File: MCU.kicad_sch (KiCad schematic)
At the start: 14 parts, among them U6 STM32F103RBTx, X1 CSTNE8M00G520000R0

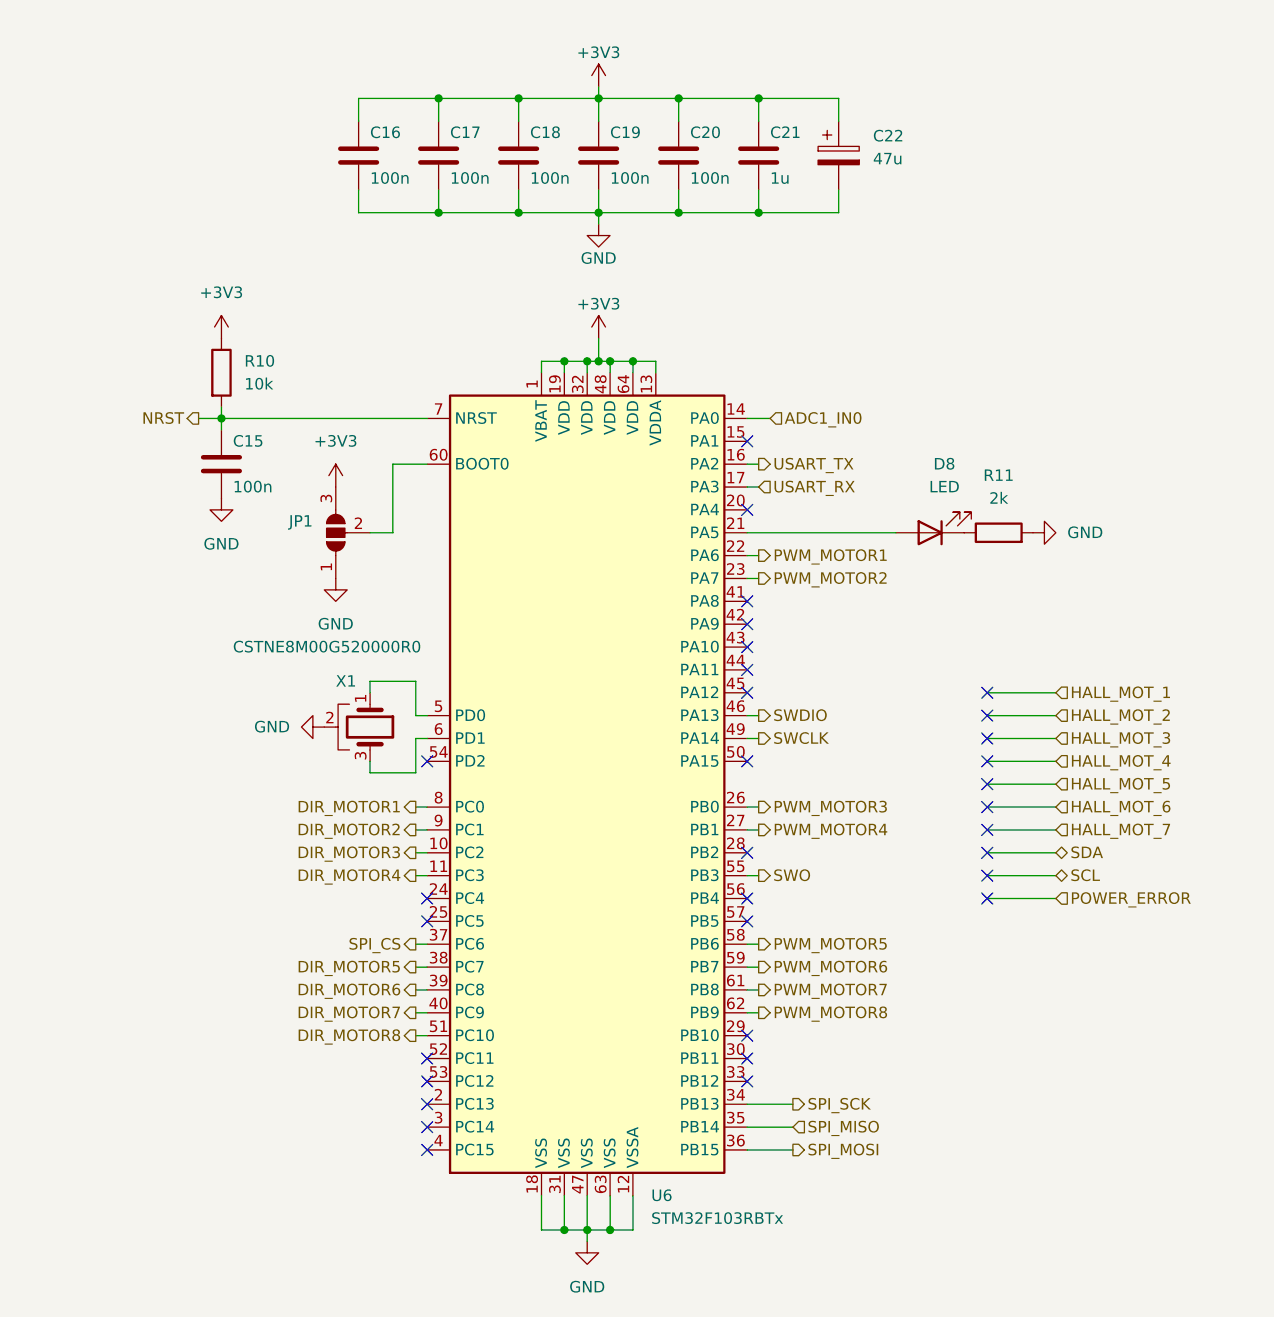
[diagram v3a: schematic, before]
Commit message: power part designed
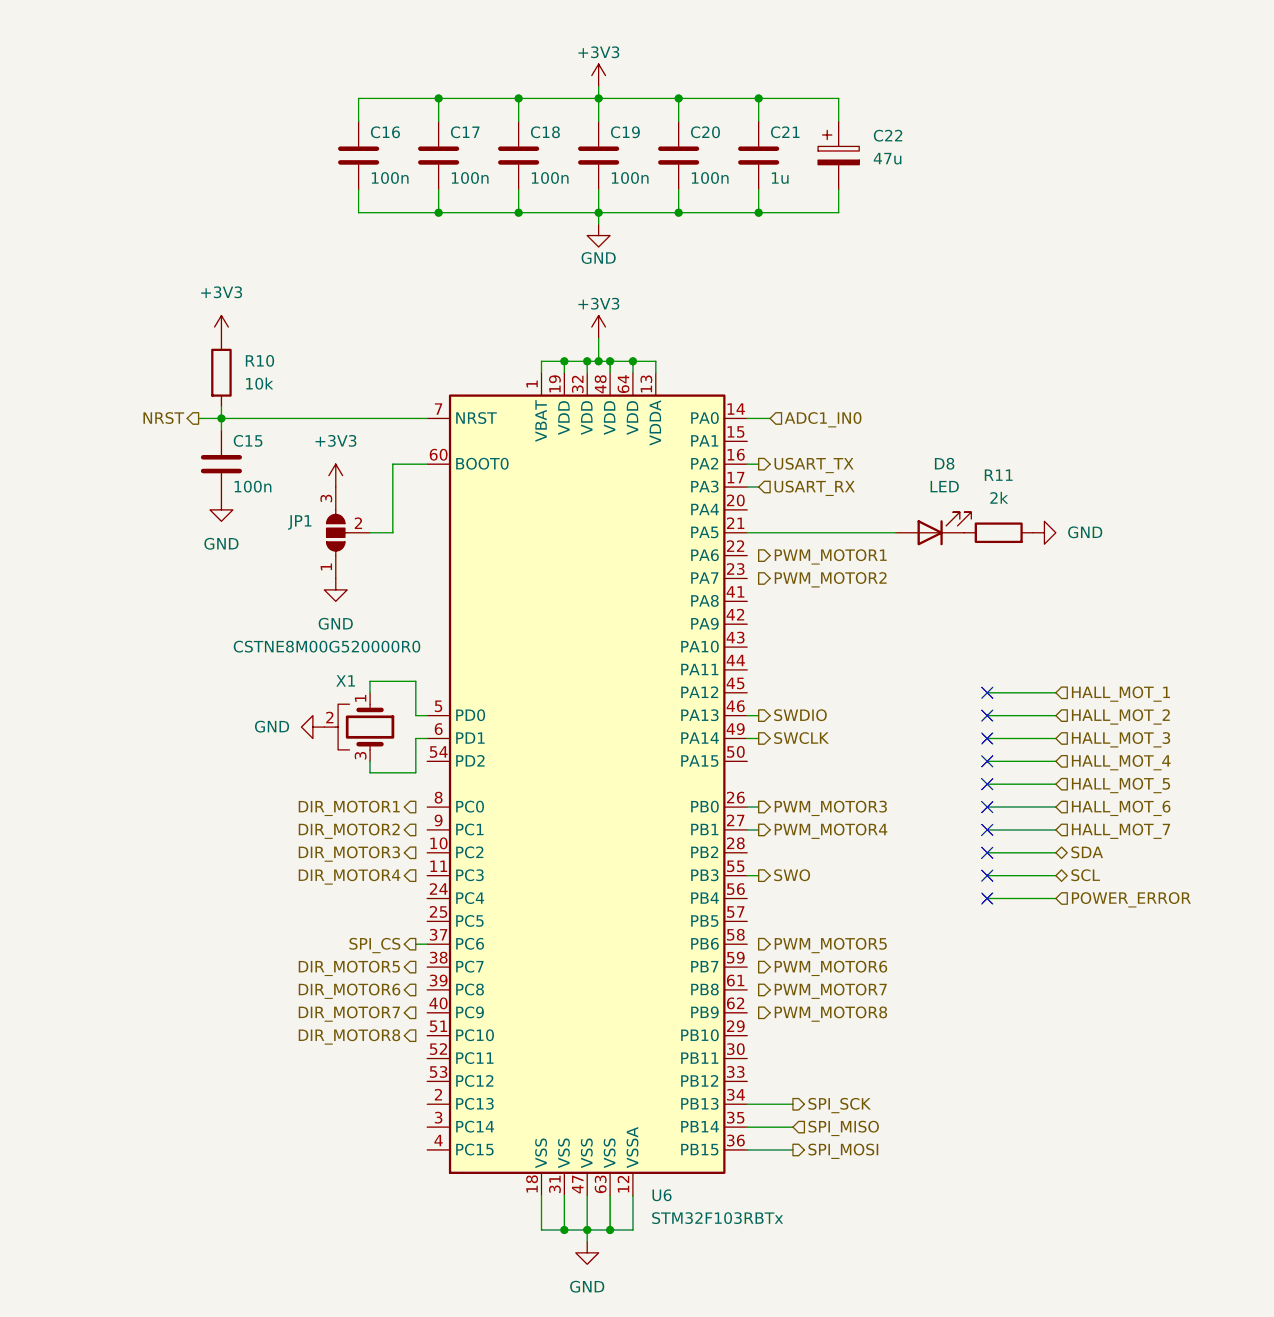
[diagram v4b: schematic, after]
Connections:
- net DIR_MOTOR1: no longer U6.8 (PC0)
- net DIR_MOTOR2: no longer U6.9 (PC1)
- net DIR_MOTOR3: no longer U6.10 (PC2)
- net DIR_MOTOR4: no longer U6.11 (PC3)
- net DIR_MOTOR5: no longer U6.38 (PC7)
- net DIR_MOTOR6: no longer U6.39 (PC8)
- net DIR_MOTOR7: no longer U6.40 (PC9)
- net DIR_MOTOR8: no longer U6.51 (PC10)
- net PWM_MOTOR1: no longer U6.22 (PA6)
- net PWM_MOTOR2: no longer U6.23 (PA7)
- net PWM_MOTOR5: no longer U6.58 (PB6)
- net PWM_MOTOR6: no longer U6.59 (PB7)
- net PWM_MOTOR7: no longer U6.61 (PB8)
- net PWM_MOTOR8: no longer U6.62 (PB9)
- no-connect marks 32 -> 10
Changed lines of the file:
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@@
   (junction (at 138.43 43.18) (diameter 0) (color 0 0 0 0)
   )
-  (no_connect (at 119.38 147.32))
-  (no_connect (at 154.94 88.9))
-  (no_connect (at 154.94 114.3))
-  (no_connect (at 154.94 86.36))
-  (no_connect (at 154.94 91.44))
-  (no_connect (at 154.94 96.52))
-  (no_connect (at 119.38 139.7))
   (no_connect (at 181.61 116.84))
   (no_connect (at 181.61 106.68))
-  (no_connect (at 119.38 144.78))
   (no_connect (at 181.61 99.06))
   (no_connect (at 181.61 109.22))
-  (no_connect (at 154.94 121.92))
-  (no_connect (at 154.94 68.58))
   (no_connect (at 181.61 114.3))
-  (no_connect (at 119.38 142.24))
-  (no_connect (at 119.38 104.14))
-  (no_connect (at 154.94 119.38))
   (no_connect (at 181.61 111.76))
-  (no_connect (at 154.94 134.62))
   (no_connect (at 181.61 119.38))
-  (no_connect (at 119.38 119.38))
-  (no_connect (at 119.38 121.92))
-  (no_connect (at 154.94 93.98))
   (no_connect (at 181.61 101.6))
-  (no_connect (at 154.94 104.14))
-  (no_connect (at 119.38 137.16))
-  (no_connect (at 154.94 137.16))
-  (no_connect (at 154.94 139.7))
   (no_connect (at 181.61 96.52))
   (no_connect (at 181.61 104.14))
-  (no_connect (at 154.94 76.2))
   (wire (pts (xy 156.21 73.66) (xy 154.94 73.66))
     (stroke (width 0) (type default) (color 0 0 0 0))
@@
     (stroke (width 0) (type default) (color 0 0 0 0))
   )
-  (wire (pts (xy 118.11 127) (xy 119.38 127))
-    (stroke (width 0) (type default) (color 0 0 0 0))
-  )
   (wire (pts (xy 181.61 96.52) (xy 189.23 96.52))
     (stroke (width 0) (type default) (color 0 0 0 0))
@@
     (stroke (width 0) (type default) (color 0 0 0 0))
   )
-  (wire (pts (xy 118.11 132.08) (xy 119.38 132.08))
-    (stroke (width 0) (type default) (color 0 0 0 0))
-  )
   (wire (pts (xy 144.78 59.69) (xy 144.78 60.96))
     (stroke (width 0) (type default) (color 0 0 0 0))
@@
     (stroke (width 0) (type default) (color 0 0 0 0))
   )
-  (wire (pts (xy 118.11 129.54) (xy 119.38 129.54))
-    (stroke (width 0) (type default) (color 0 0 0 0))
-  )
   (wire (pts (xy 138.43 30.48) (xy 138.43 33.02))
     (stroke (width 0) (type default) (color 0 0 0 0))
   )
-  (wire (pts (xy 156.21 81.28) (xy 154.94 81.28))
-    (stroke (width 0) (type default) (color 0 0 0 0))
-  )
   (wire (pts (xy 156.21 30.48) (xy 156.21 33.02))
     (stroke (width 0) (type default) (color 0 0 0 0))
@@
     (stroke (width 0) (type default) (color 0 0 0 0))
   )
-  (wire (pts (xy 118.11 114.3) (xy 119.38 114.3))
-    (stroke (width 0) (type default) (color 0 0 0 0))
-  )
   (wire (pts (xy 160.02 144.78) (xy 154.94 144.78))
     (stroke (width 0) (type default) (color 0 0 0 0))
@@
     (stroke (width 0) (type default) (color 0 0 0 0))
   )
-  (wire (pts (xy 156.21 132.08) (xy 154.94 132.08))
-    (stroke (width 0) (type default) (color 0 0 0 0))
-  )
   (wire (pts (xy 139.7 59.69) (xy 139.7 60.96))
     (stroke (width 0) (type default) (color 0 0 0 0))
@@
     (stroke (width 0) (type default) (color 0 0 0 0))
   )
-  (wire (pts (xy 118.11 134.62) (xy 119.38 134.62))
-    (stroke (width 0) (type default) (color 0 0 0 0))
-  )
   (wire (pts (xy 181.61 114.3) (xy 189.23 114.3))
     (stroke (width 0) (type default) (color 0 0 0 0))
@@
     (stroke (width 0) (type default) (color 0 0 0 0))
   )
-  (wire (pts (xy 156.21 127) (xy 154.94 127))
-    (stroke (width 0) (type default) (color 0 0 0 0))
-  )
   (wire (pts (xy 134.62 156.21) (xy 137.16 156.21))
     (stroke (width 0) (type default) (color 0 0 0 0))
   )
-  (wire (pts (xy 156.21 129.54) (xy 154.94 129.54))
-    (stroke (width 0) (type default) (color 0 0 0 0))
-  )
   (wire (pts (xy 120.65 30.48) (xy 120.65 33.02))
     (stroke (width 0) (type default) (color 0 0 0 0))
   )
-  (wire (pts (xy 118.11 116.84) (xy 119.38 116.84))
-    (stroke (width 0) (type default) (color 0 0 0 0))
-  )
   (wire (pts (xy 96.52 66.04) (xy 96.52 67.31))
     (stroke (width 0) (type default) (color 0 0 0 0))
@@
     (stroke (width 0) (type default) (color 0 0 0 0))
   )
-  (wire (pts (xy 156.21 83.82) (xy 154.94 83.82))
-    (stroke (width 0) (type default) (color 0 0 0 0))
-  )
   (wire (pts (xy 96.52 66.04) (xy 119.38 66.04))
     (stroke (width 0) (type default) (color 0 0 0 0))
   )
-  (wire (pts (xy 118.11 109.22) (xy 119.38 109.22))
-    (stroke (width 0) (type default) (color 0 0 0 0))
-  )
   (wire (pts (xy 156.21 101.6) (xy 154.94 101.6))
     (stroke (width 0) (type default) (color 0 0 0 0))
@@
     (stroke (width 0) (type default) (color 0 0 0 0))
   )
-  (wire (pts (xy 118.11 111.76) (xy 119.38 111.76))
-    (stroke (width 0) (type default) (color 0 0 0 0))
-  )
   (wire (pts (xy 147.32 33.02) (xy 147.32 30.48))
     (stroke (width 0) (type default) (color 0 0 0 0))
@@
     (stroke (width 0) (type default) (color 0 0 0 0))
   )
-  (wire (pts (xy 156.21 124.46) (xy 154.94 124.46))
-    (stroke (width 0) (type default) (color 0 0 0 0))
-  )

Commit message: added pull-ups to the logic gates
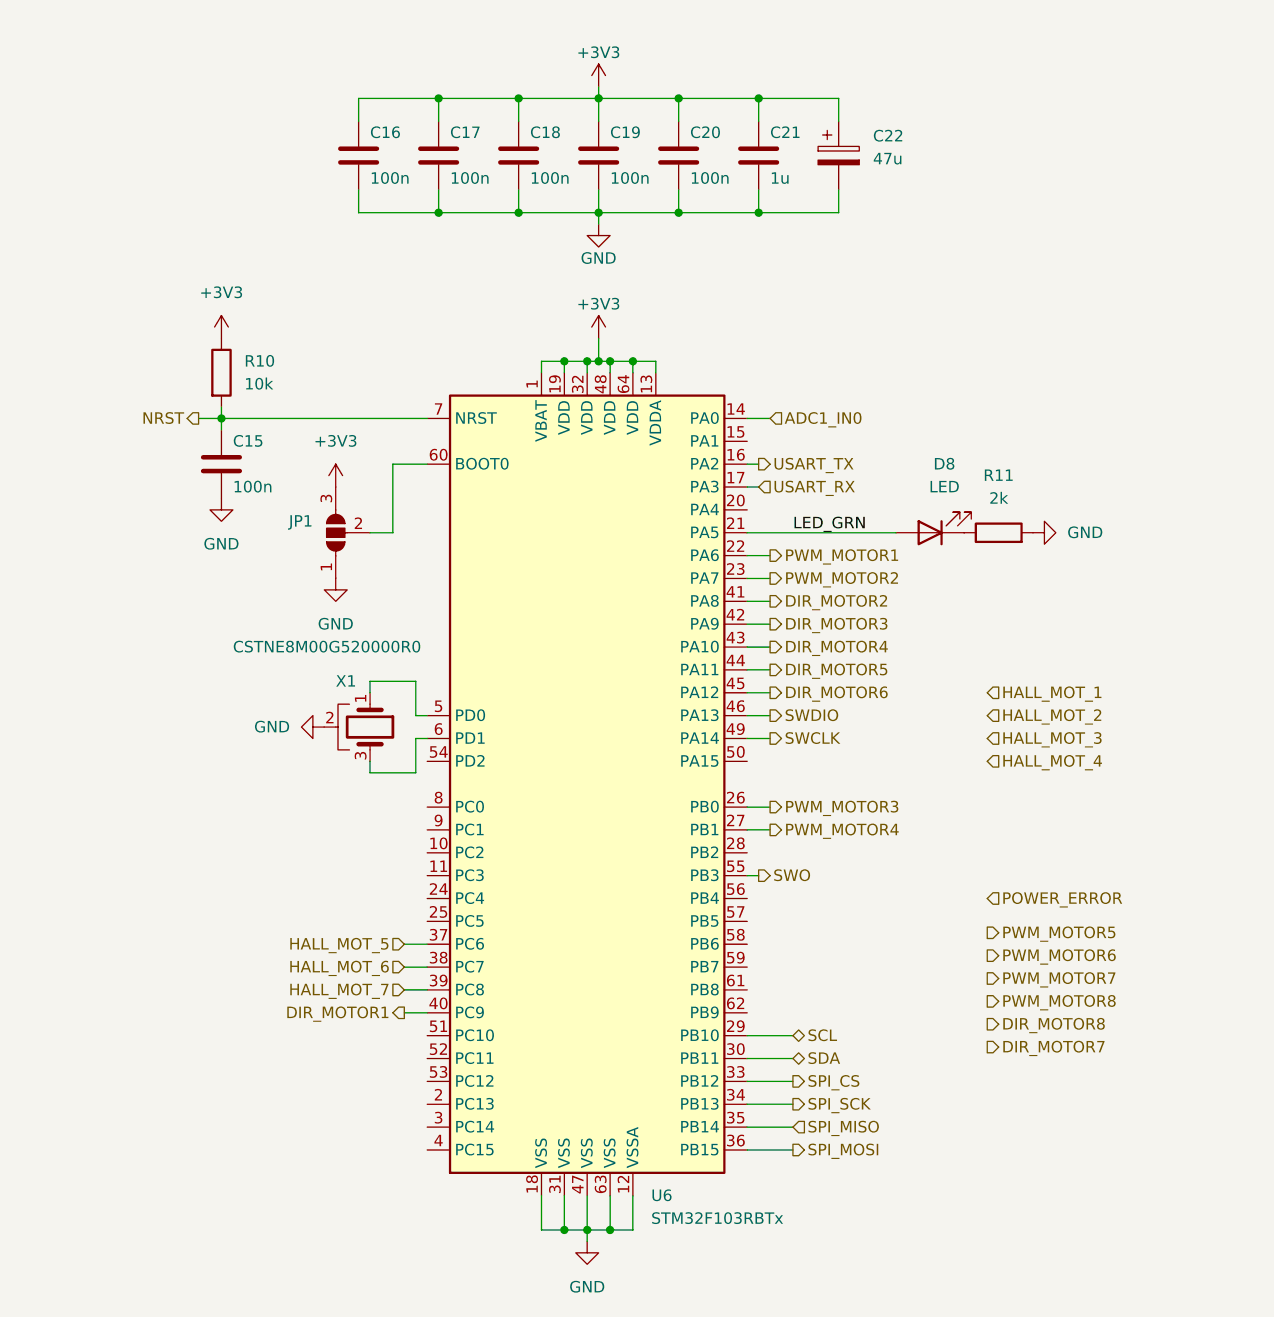
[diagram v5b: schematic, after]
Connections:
- net DIR_MOTOR1: now also U6.40 (PC9)
- net DIR_MOTOR2: now also U6.41 (PA8)
- net DIR_MOTOR3: now also U6.42 (PA9)
- net DIR_MOTOR4: now also U6.43 (PA10)
- net DIR_MOTOR5: now also U6.44 (PA11)
- net DIR_MOTOR6: now also U6.45 (PA12)
- net HALL_MOT_5: now also U6.37 (PC6)
- net HALL_MOT_6: now also U6.38 (PC7)
- net HALL_MOT_7: now also U6.39 (PC8)
- net PWM_MOTOR1: now also U6.22 (PA6)
- net PWM_MOTOR2: now also U6.23 (PA7)
- net SCL: now also U6.29 (PB10)
- net SDA: now also U6.30 (PB11)
- net SPI_CS: now also U6.33 (PB12); no longer U6.37 (PC6)
- net LED_GRN: now reaches D8.2 (A), U6.21 (PA5)
- no-connect marks 10 -> 0

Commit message: ADC resistors and outputs added
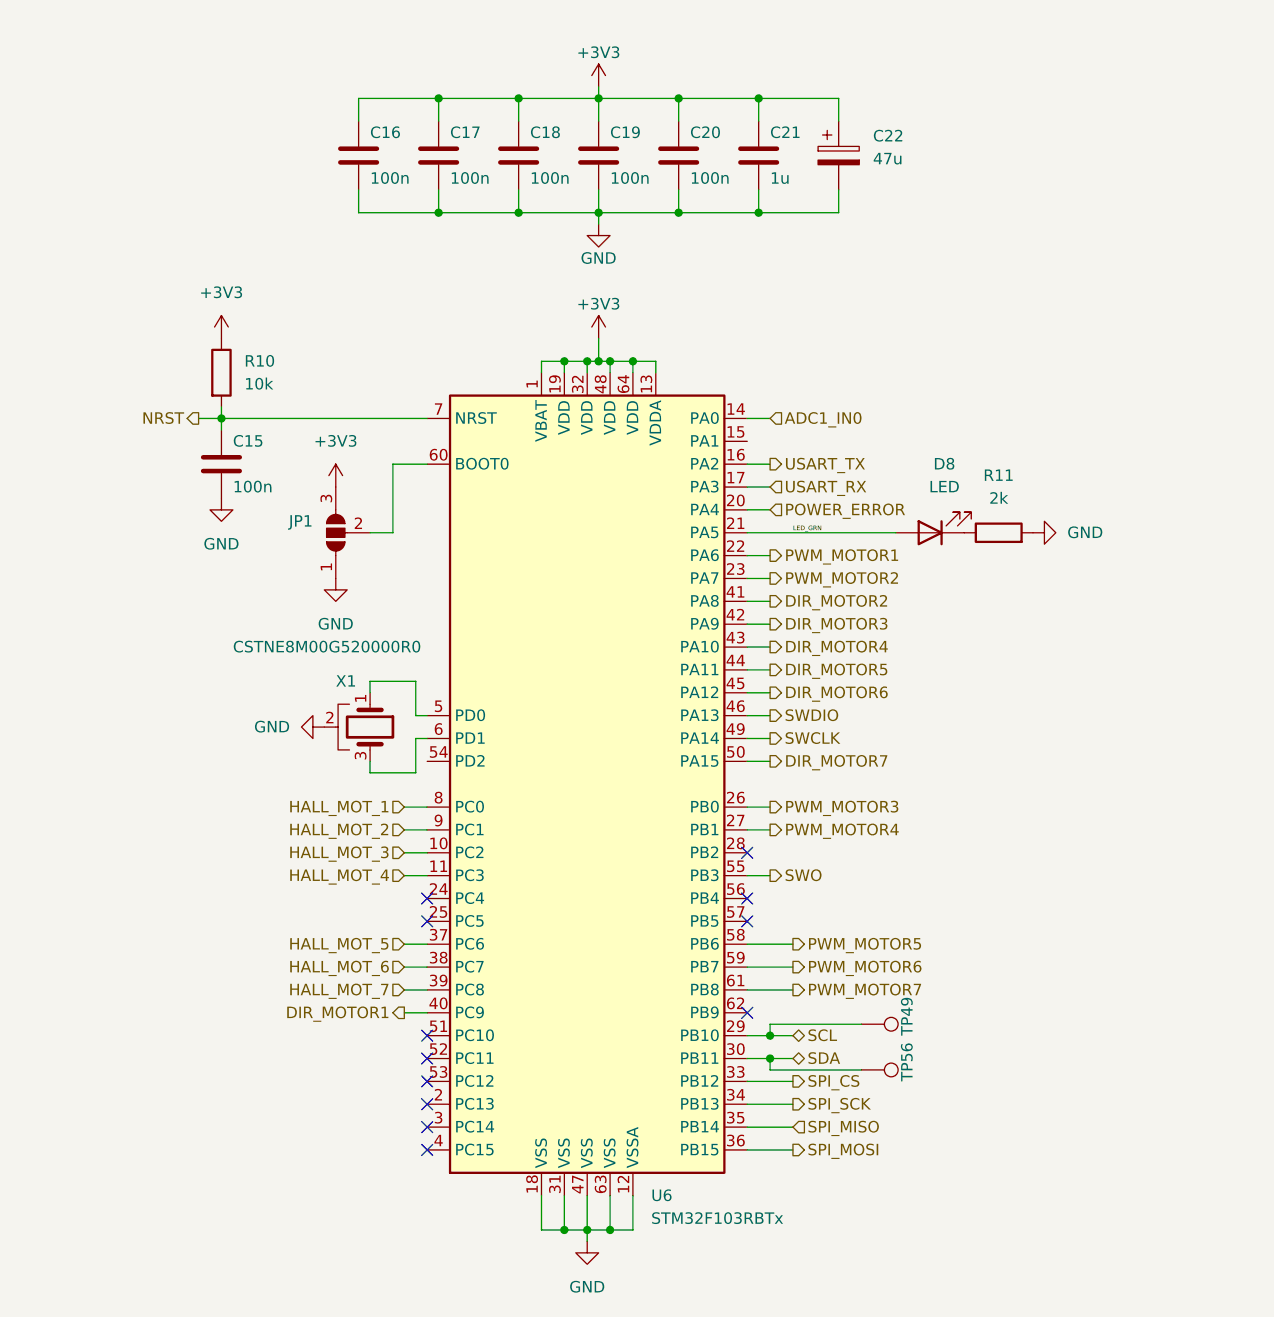
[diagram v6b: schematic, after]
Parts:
- added TP49, TP56: TestPoint, TestPoint:TestPoint_THTPad_1.0x1.0mm_Drill0.5mm, symbol Connector:TestPoint
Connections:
- net DIR_MOTOR7: now also U6.50 (PA15)
- net HALL_MOT_1: now also U6.8 (PC0)
- net HALL_MOT_2: now also U6.9 (PC1)
- net HALL_MOT_3: now also U6.10 (PC2)
- net HALL_MOT_4: now also U6.11 (PC3)
- net POWER_ERROR: now also U6.20 (PA4)
- net PWM_MOTOR5: now also U6.58 (PB6)
- net PWM_MOTOR6: now also U6.59 (PB7)
- net PWM_MOTOR7: now also U6.61 (PB8)
- net SCL: now also TP49.1
- net SDA: now also TP56.1
- no-connect marks 0 -> 12

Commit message: v2.1 finished
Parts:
- removed X1: CSTNE8M00G520000R0, _Others:CSTNE8M00G520000R0, symbol _others:CSTNE8M00G520000R0
- added C78, C79, C80: 100n, Capacitor_SMD:C_0603_1608Metric_Pad1.08x0.95mm_HandSolder, symbol Device:C
- added C81: 1u, Capacitor_SMD:C_0603_1608Metric_Pad1.08x0.95mm_HandSolder, symbol Device:C
- added FB1: FerriteBead, Resistor_SMD:R_0603_1608Metric_Pad0.98x0.95mm_HandSolder, symbol Device:FerriteBead
- added Y1: LFXTAL026380, _Others:LFXTAL026380, symbol _others:LFXTAL026380
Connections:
- net +3V3: now also FB1.1; no longer U6.13 (VDDA)
- net GND: now also C78.2, C79.2, C80.2, C81.2, Y1.2, Y1.4
- net at U6.5 (PD0): now also C78.1, Y1.1
- net at U6.6 (PD1): now also C79.1, Y1.3
- new net VDDA: C80.1, C81.1, FB1.2, U6.13 (VDDA)
- no-connect marks 12 -> 13
